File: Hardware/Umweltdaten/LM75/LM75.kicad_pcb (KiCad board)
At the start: 2 copper layers, 6 parts, among them IC2 LM75, P1 I2C

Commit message: LM/TMP75 layout
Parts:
- added R1: 10k, Resistors_SMD:R_0805_HandSoldering, F.Cu at (154.9, 113.0)
- added R2: 10k, Resistors_SMD:R_0805_HandSoldering, F.Cu at (154.9, 108.0)
- added R3: 10k, Resistors_SMD:R_0805_HandSoldering, F.Cu at (156.2, 104.1)
- moved C1 2.54 mm to (163.8, 104.1)
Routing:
- net +3V3: track 0.00 -> 48.2 mm
- net Net-(IC2-Pad1): track 13.5 -> 3.40 mm
- net Net-(IC2-Pad2): track 9.72 -> 4.37 mm
- net GND: track 4.34 -> 9.05 mm, vias 0 -> 15
- net Net-(IC2-Pad3): track 7.03 -> 5.57 mm
- net Net-(IC2-Pad5): track 5.87 -> 7.06 mm
- net Net-(IC2-Pad7): track 7.14 -> 7.70 mm
- added copper zone on B.Cu, net GND
- added copper zone on F.Cu, net GND
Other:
- board outline added: 22 x 16 mm
- net class Default: clearance 0.2 -> 0.2032; trace_width 0.5 -> 0.508
- rule trace_clearance: 0.2 -> 0.2032
- rule via_min_size: 0.4 -> 0.5

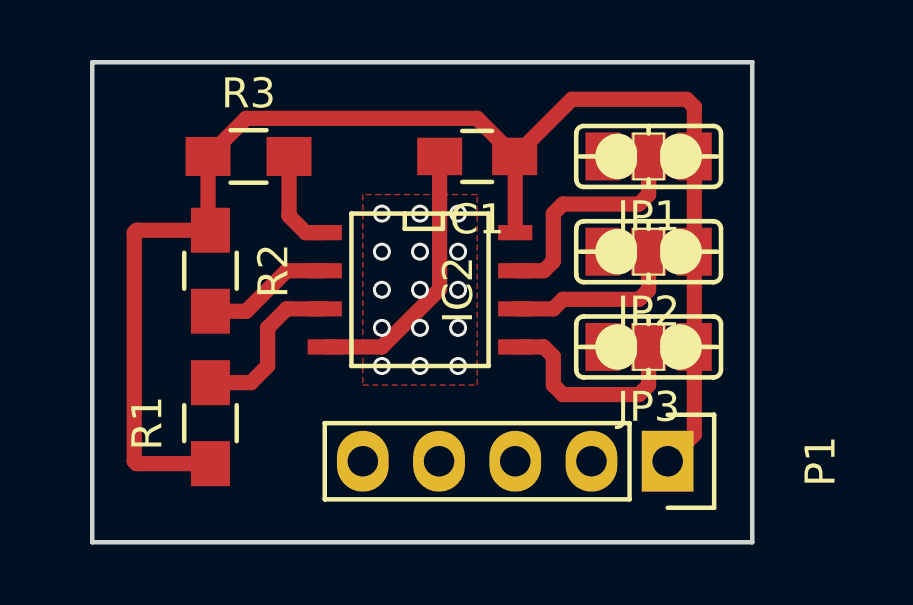
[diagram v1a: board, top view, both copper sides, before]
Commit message: finished LM/TMP75 PCB
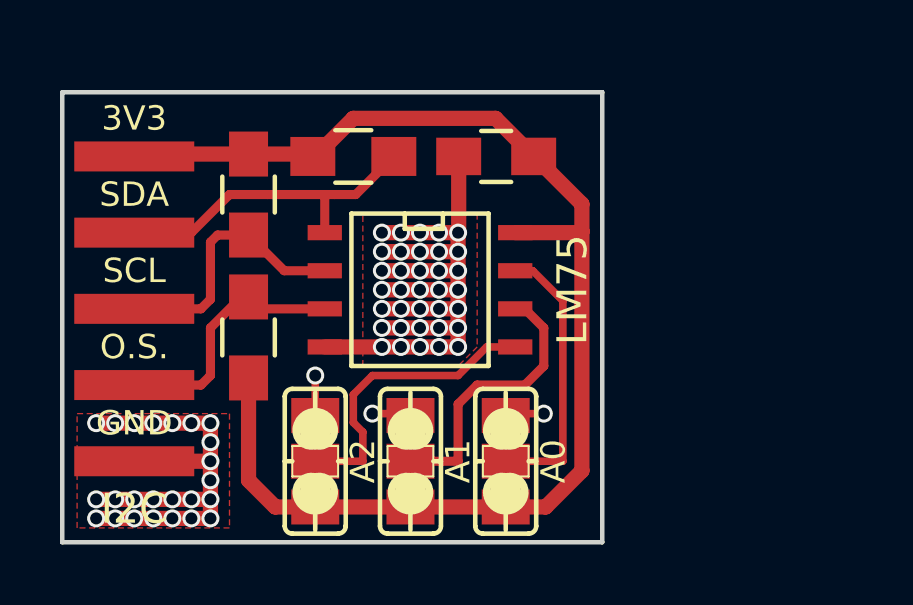
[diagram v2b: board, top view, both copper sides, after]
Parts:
- P1: footprint Pin_Headers:Pin_Header_Straight_1x05 -> SMD:SMD_05-4mm
- moved P1 20.5 mm to (152.4, 104.1), turned to 0 degrees
- moved JP3 11.7 mm to (158.4, 114.3), turned to 90 degrees
- moved JP1 11.2 mm to (164.8, 114.3), turned to 90 degrees
- moved JP2 10.6 mm to (161.6, 114.3), turned to 90 degrees
- moved R3 3.49 mm to (159.7, 104.1)
- moved R1 3.13 mm to (156.2, 110.2)
- moved R2 2.84 mm to (156.2, 105.4)
- moved C1 0.63 mm to (164.5, 104.1)
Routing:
- net GND: track 9.05 -> 47.7 mm, vias 15 -> 62
- net Net-(IC2-Pad1): track 3.40 -> 11.0 mm
- net Net-(IC2-Pad2): track 4.37 -> 8.98 mm
- net +3V3: track 48.2 -> 44.3 mm
- net Net-(IC2-Pad6): track 5.98 -> 9.36 mm
- net Net-(IC2-Pad3): track 5.57 -> 8.66 mm
- net Net-(IC2-Pad5): track 7.06 -> 10.00 mm
- net Net-(IC2-Pad7): track 7.70 -> 9.25 mm
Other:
- board size 22 x 16 mm -> 18 x 15 mm
- rule trace_min: 0.2 -> 0.2032
- rule via_min_size: 0.5 -> 0.0254
- board text added: "3V3"
- board text added: "A0"
- board text added: "A1"
- board text added: "A2"
- board text added: "GND"
- board text added: "O.S."
- board text added: "SCL"
- board text added: "SDA"

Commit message: create Gerber files
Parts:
- moved C1 181.4 mm to (14.5, 2.14)
- moved IC2 181.4 mm to (11.9, 6.58)
- moved JP1 181.4 mm to (14.8, 12.3)
- moved JP2 181.4 mm to (11.6, 12.3)
- moved JP3 181.4 mm to (8.43, 12.3)
- moved P1 181.4 mm to (2.40, 2.14)
- moved R1 181.4 mm to (6.21, 8.17)
- moved R2 181.4 mm to (6.21, 3.41)
- moved R3 181.4 mm to (9.70, 2.14)
